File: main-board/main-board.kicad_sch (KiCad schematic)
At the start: 56 parts, among them J1 Conn_02x08_Odd_Even, J2 7-12V, Q1 AO3400A, Q2 AO3400A, Q3 AO3400A, Q4 AO3400A, Q5 AO3400A, Q6 AO3400A, Q7 AO3400A, Q8 AO3400A, U1 CD40106B, U2 CD4024B, U3 CD4040B, U4 27C256, U5 LM78L05, U6 ULN2803A, U7 CD4028B

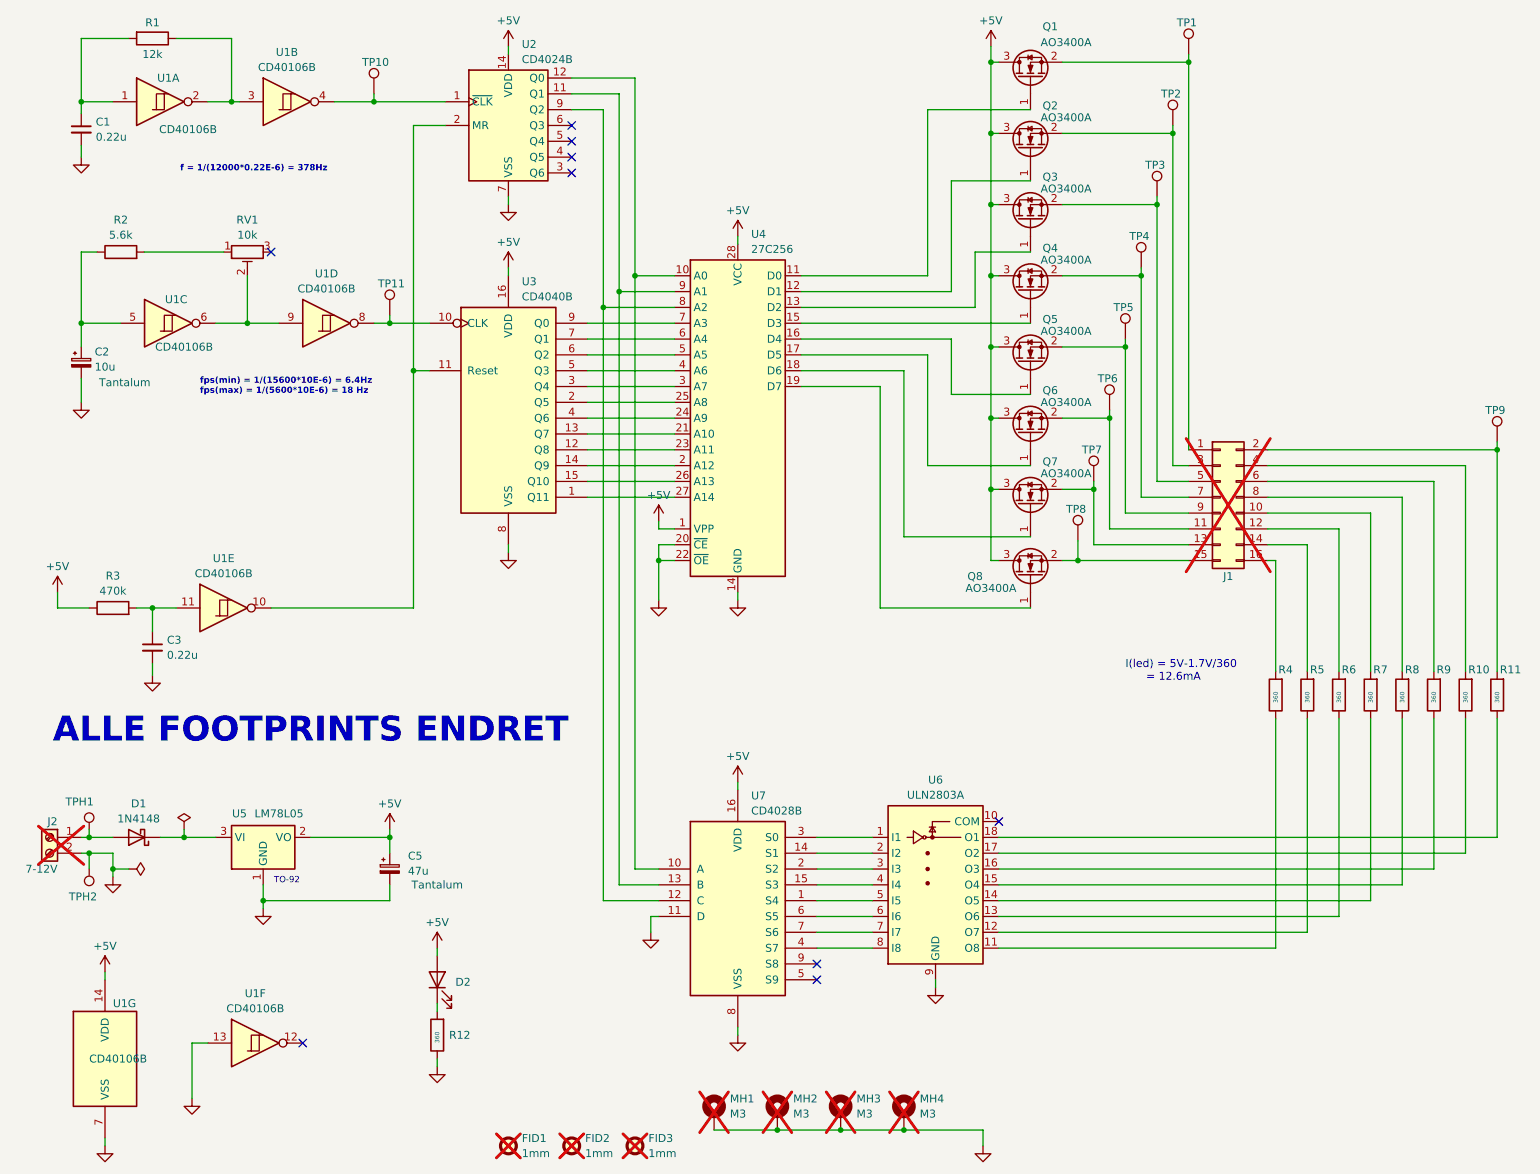
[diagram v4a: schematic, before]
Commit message: completed routing of smd board
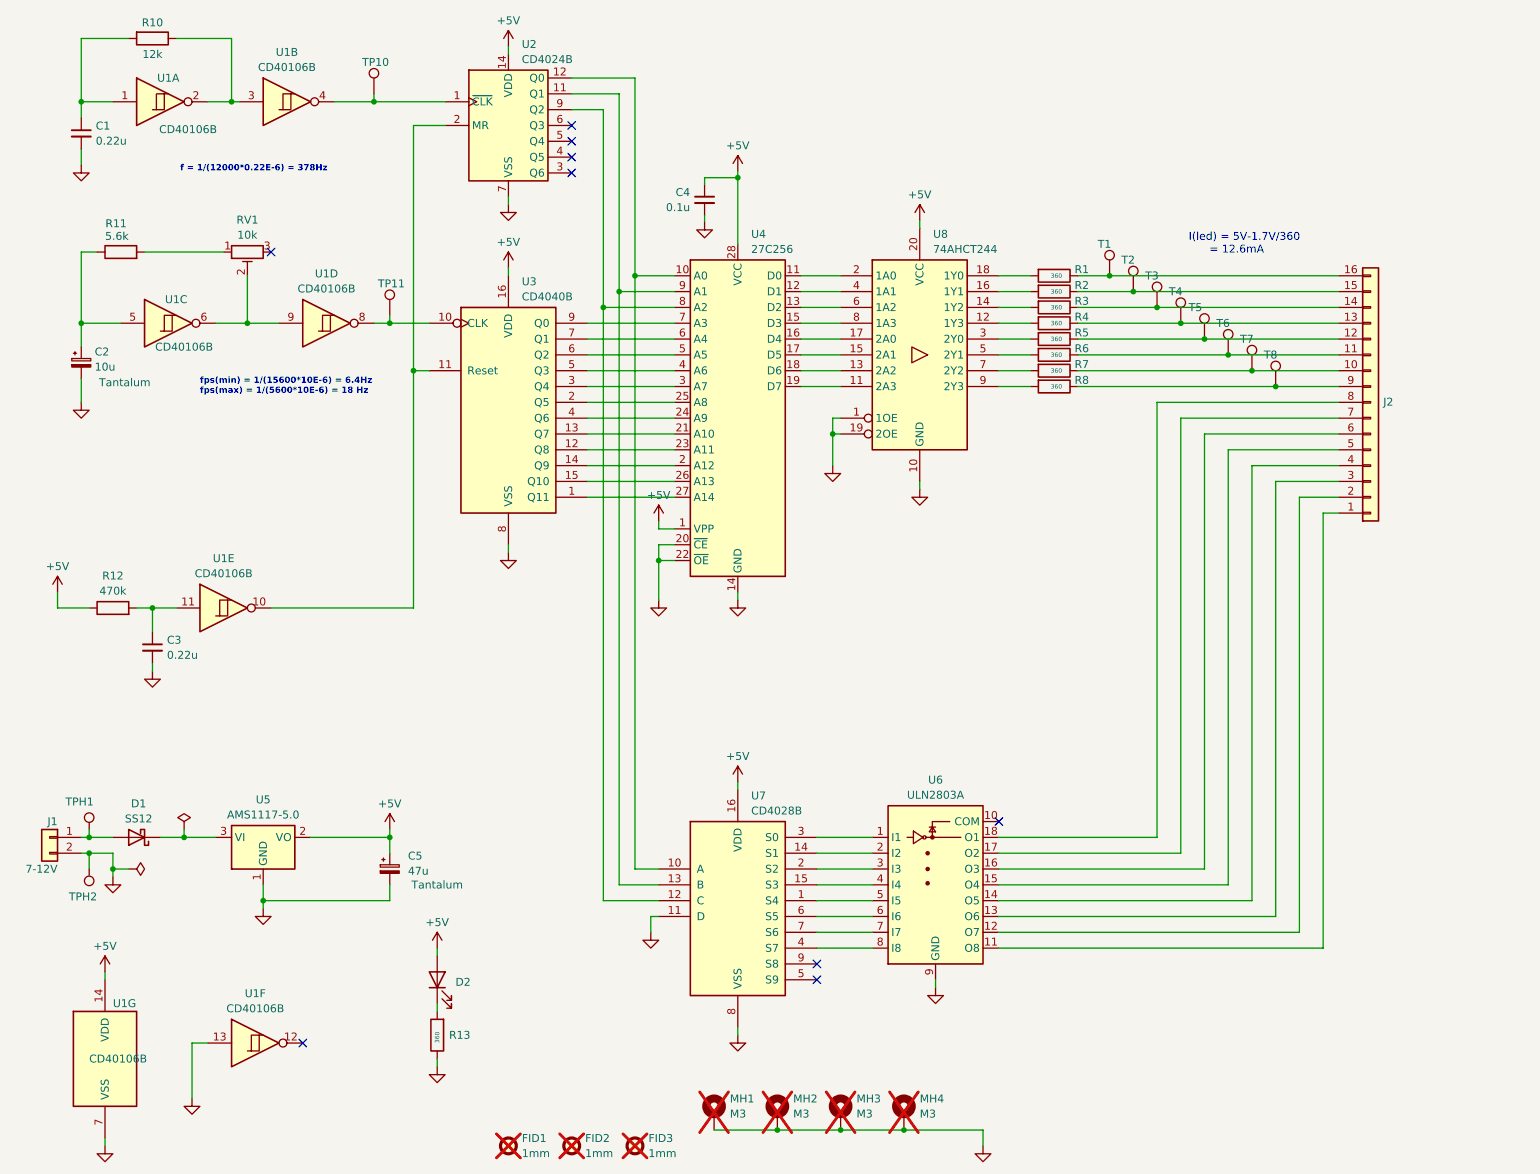
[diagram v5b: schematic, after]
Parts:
- removed J1: Conn_02x08_Odd_Even, Connector_PinHeader_2.54mm:PinHeader_2x08_P2.54mm_Horizontal, symbol Connector_Generic:Conn_02x08_Odd_Even
- removed Q1, Q2, Q3, Q4, Q5, Q6, Q7, Q8: AO3400A, Package_TO_SOT_SMD:SOT-23, symbol Transistor_FET:AO3400A
- removed TP8, TP9: TestPoint, ezee-footprints:TestPoint_Pad_D1.0mm, symbol Connector:TestPoint
- added C4: 0.1u, Capacitor_SMD:C_0603_1608Metric_Pad1.08x0.95mm_HandSolder, symbol Device:C_Small
- added J2: Conn_01x16, Connector_FFC-FPC:TE_1-84952-6_1x16-1MP_P1.0mm_Horizontal, symbol Connector_Generic:Conn_01x16
- added T8: TestPoint, ezee-footprints:TestPoint_Pad_D1.0mm, symbol Connector:TestPoint
- added U8: 74AHCT244, Package_SO:TSSOP-20_4.4x6.5mm_P0.65mm, symbol 74xx:74AHCT244
- D1: value 1N4148 -> SS12
- D2: footprint LED_SMD:LED_0805_2012Metric_Pad1.15x1.40mm_HandSolder -> LED_SMD:LED_1206_3216Metric_Pad1.42x1.75mm_HandSolder
- J1: renamed from J2; footprint ezee-footprints:Battery_Terminals -> Connector_JST:JST_PH_S2B-PH-K_1x02_P2.00mm_Horizontal; symbol Connector:Screw_Terminal_01x02 -> Connector_Generic:Conn_01x02; now fitted; now in the parts list
- TPH1, TPH2: footprint ezee-footprints:TestPoint_Hook -> ezee-footprints:LUG_3mm_W4mm
- U5: value LM78L05 -> AMS1117-5.0
- renumbered R4 to R1, R1 to R10, R2 to R11, R3 to R12, R12 to R13, R5 to R2, R6 to R3, R7 to R4, R8 to R5, R9 to R6, R10 to R7, R11 to R8, TP1 to T1, TP2 to T2, TP3 to T3, TP4 to T4, TP5 to T5, TP6 to T6, TP7 to T7
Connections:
- net +5V: now also C4.1, U8.20 (VCC)
- net GND: now also C4.2, U8.1 (1OE), U8.10 (GND), U8.19 (2OE)
- net at R8.2: now also U8.9 (2Y3)
- net at T7.1: now also R7.1, J2.10 (Pin_10)
- net at U4.13 (D2): now also U8.6 (1A2)
- net at T3.1: now also R3.1, J2.14 (Pin_14)
- net at R4.1: now also T4.1, J2.13 (Pin_13); no longer U6.14 (O5)
- net at R4.2: now also U8.12 (1Y3)
- net at U6.13 (O6): now also J2.3 (Pin_3); no longer R3.1
- net at R3.2: now also U8.14 (1Y2)
- net at T2.1: now also R2.1, J2.15 (Pin_15)
- net at U4.11 (D0): now also U8.2 (1A0)
- net at U4.12 (D1): now also U8.4 (1A1)
- net at U4.15 (D3): now also U8.8 (1A3)
- net at U4.16 (D4): now also U8.17 (2A0)
- net at U4.17 (D5): now also U8.15 (2A1)
- net at U4.18 (D6): now also U8.13 (2A2)
- net at U4.19 (D7): now also U8.11 (2A3)
- net at T6.1: now also R6.1, J2.11 (Pin_11)
- net at R1.1: now also T1.1, J2.16 (Pin_16); no longer U6.11 (O8)
- net at R1.2: now also U8.18 (1Y0)
- net at R8.1: now also J2.9 (Pin_9), T8.1; no longer U6.18 (O1)
- net at U6.12 (O7): now also J2.2 (Pin_2); no longer R2.1
- net at R2.2: now also U8.16 (1Y1)
- net at R5.1: now also T5.1, J2.12 (Pin_12); no longer U6.15 (O4)
- net at R5.2: now also U8.3 (2Y0)
- net at U6.16 (O3): now also J2.6 (Pin_6); no longer R6.1
- net at R6.2: now also U8.5 (2Y1)
- net at R7.2: now also U8.7 (2Y2)
- net at U6.17 (O2): now also J2.7 (Pin_7); no longer R7.1
- new net: J2.1 (Pin_1), U6.11 (O8)
- new net: J2.4 (Pin_4), U6.14 (O5)
- new net: J2.5 (Pin_5), U6.15 (O4)
- new net: J2.8 (Pin_8), U6.18 (O1)
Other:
- note removed: "ALLE FOOTPRINTS ENDRET"
- note removed: "TO-92"
- moved on the sheet: C1, R1, R2, R3, R4, R5, R6, R7, R8, T1, T2, T3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

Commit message: footprint fixes etc
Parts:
- removed TPH1, TPH2: TestPoint_Hook, ezee-footprints:LUG_3mm_W4mm, symbol ezee-symbols:TestPoint_Hook
- added TPH1, TPH2: TestPoint_Hook, kicad-ezee-footprints:TestPoint_Hook, symbol kicad-ezee-symbols:TestPoint_Hook
- C1: value 0.22u -> 1u
- C2: value 10u -> 4.7u; footprint Capacitor_Tantalum_SMD:CP_EIA-7343-20_Kemet-V -> Capacitor_Tantalum_SMD:CP_EIA-6032-15_Kemet-U
- C3: value 0.22u -> 390n; footprint Capacitor_SMD:C_0603_1608Metric_Pad1.08x0.95mm_HandSolder -> Capacitor_SMD:C_0805_2012Metric_Pad1.18x1.45mm_HandSolder
- C5: footprint Capacitor_Tantalum_SMD:CP_EIA-7343-20_Kemet-V -> Capacitor_Tantalum_SMD:CP_EIA-6032-15_Kemet-U
- R1, R13, R2, R3, R4, R5, R6, R7, R8: value 360 -> 200; footprint Capacitor_SMD:C_0603_1608Metric_Pad1.08x0.95mm_HandSolder -> Resistor_SMD:R_0805_2012Metric_Pad1.20x1.40mm_HandSolder
- R10: value 12k -> 470; footprint Resistor_SMD:R_0603_1608Metric_Pad0.98x0.95mm_HandSolder -> Resistor_SMD:R_0805_2012Metric_Pad1.20x1.40mm_HandSolder
- R11: value 5.6k -> 4.7k; footprint Capacitor_SMD:C_0603_1608Metric_Pad1.08x0.95mm_HandSolder -> Resistor_SMD:R_0805_2012Metric_Pad1.20x1.40mm_HandSolder
- R12: footprint Capacitor_SMD:C_0603_1608Metric_Pad1.08x0.95mm_HandSolder -> Resistor_SMD:R_0805_2012Metric_Pad1.20x1.40mm_HandSolder
- RV1: value 10k -> 100k; footprint ezee-footprints:Potentiometer_Wheel_3pin_Pitch4mm -> kicad-ezee-footprints:Potentiometer_Wheel_3pin_Pitch4mm
- T1, T2, T3, T4, T5, T6, T7, T8, TP10, TP11: footprint ezee-footprints:TestPoint_Pad_D1.0mm -> kicad-ezee-footprints:TestPoint_Pad_1.0x1.0mm
- U8: PartNo (none) -> MM74HCT244MTCX
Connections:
- net GND: now also TPH2.1
- net at D1.2 (A), J1.1 (Pin_1): now also TPH1.1
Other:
- note added: "I(led) = 10mA V(led) = 2V I(2803) = 1V R = (5V-1V-2V)/0.01 = 200 ohm"
- note added: "f = 1/(470*1E-6) = 2178Hz"
- note added: "fps(min) = 1/( (4.7k+100k) * 4.7E-6) = 2Hz fps(max) = 1/(4.7k*4.7E-6) = 45Hz"
- note removed: "I(led) = 5V-1.7V/360 = 12.6mA"
- note removed: "f = 1/(12000*0.22E-6) = 378Hz"
- note removed: "fps(min) = 1/(15600*10E-6) = 6.4Hz fps(max) = 1/(5600*10E-6) = 18 Hz"
- moved on the sheet: C4, U1F
